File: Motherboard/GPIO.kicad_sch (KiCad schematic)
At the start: 12 parts, among them J19 BM04B-NSHSS-TBT_LF__SN_, J20 BM04B-NSHSS-TBT_LF__SN_, J50 5034801400, J51 5034801400, J52 503480-0800

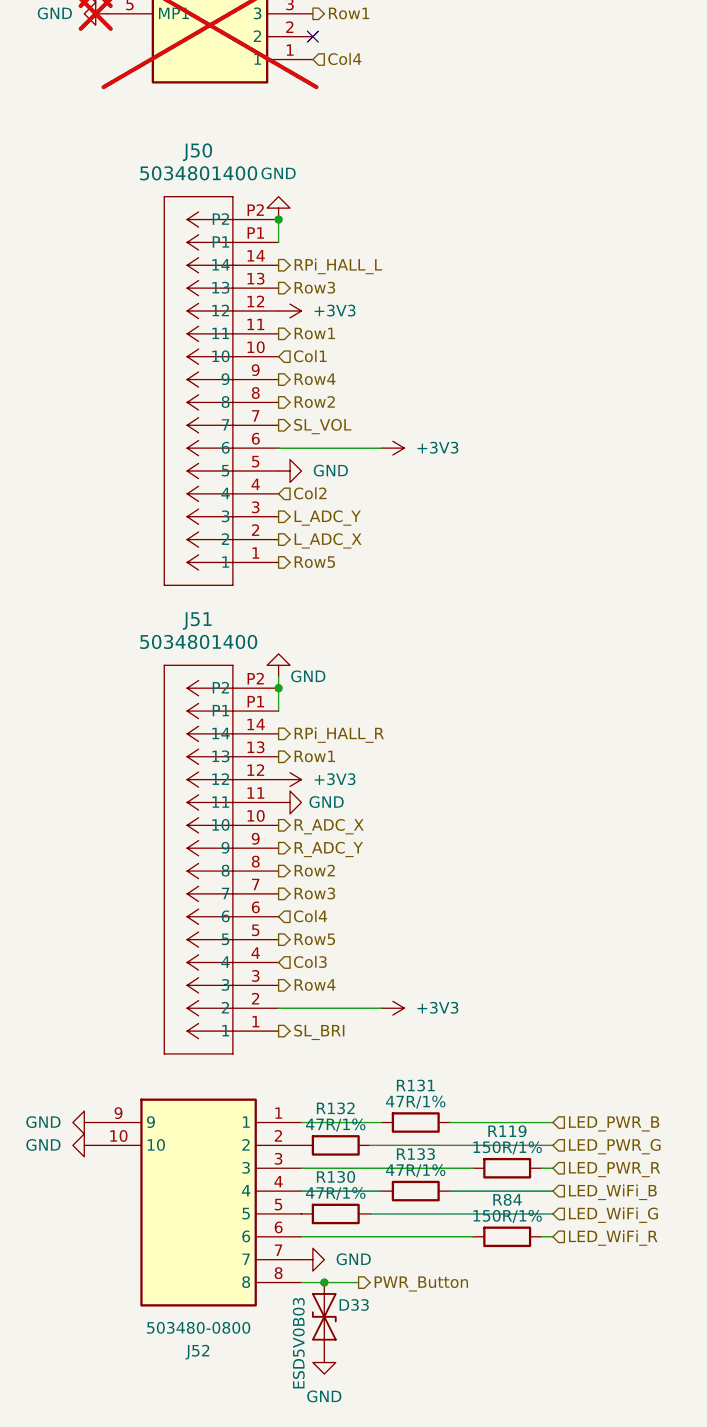
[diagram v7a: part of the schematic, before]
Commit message: Performed analysis of current work. Documented motherboard issues, new revision Todo
- Also updated README
- Other stuff
- 3D Modeling in progress
- Nothing significant done, just want to break the lack of updates.

Project aim to finish before 2027, otherwise no further deadline will be set.
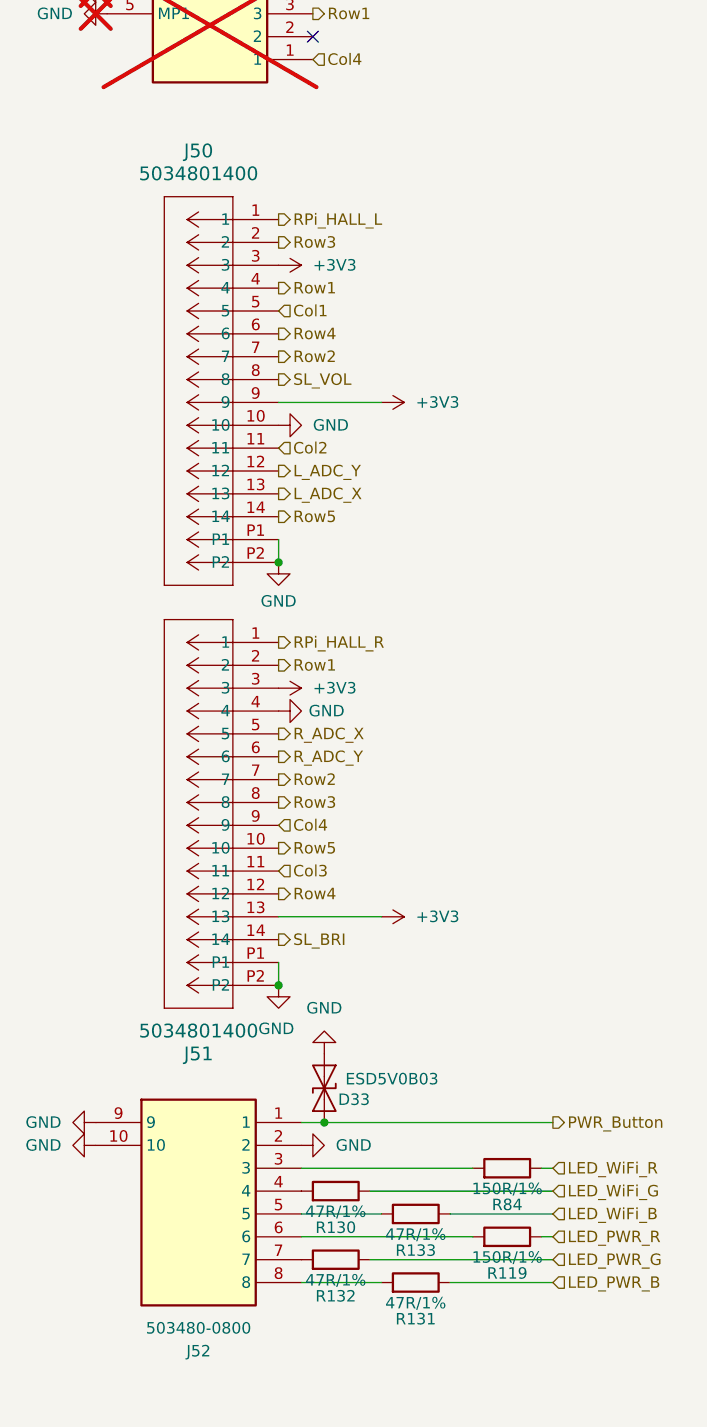
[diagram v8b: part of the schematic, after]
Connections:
- net +3V3: now also J50.3, J50.9, J51.13, J51.3; no longer J50.12, J50.6, J51.12, J51.2
- net Col1: now also J50.5; no longer J50.10
- net Col2: now also J50.11; no longer J50.4
- net Col3: now also J51.11; no longer J51.4
- net Col4: now also J51.9; no longer J51.6
- net GND: now also J50.10, J51.4, J52.2; no longer J50.5, J51.11, J52.7
- net L_ADC_X: now also J50.13; no longer J50.2
- net L_ADC_Y: now also J50.12; no longer J50.3
- net PWR_Button: now also J52.1; no longer J52.8
- net RPi_HALL_L: now also J50.1; no longer J50.14
- net RPi_HALL_R: now also J51.1; no longer J51.14
- net R_ADC_X: now also J51.5; no longer J51.10
- net R_ADC_Y: now also J51.6; no longer J51.9
- net Row1: now also J50.4, J51.2; no longer J50.11, J51.13
- net Row2: now also J50.7, J51.7; no longer J50.8, J51.8
- net Row3: now also J50.2, J51.8; no longer J50.13, J51.7
- net Row4: now also J50.6, J51.12; no longer J50.9, J51.3
- net Row5: now also J50.14, J51.10; no longer J50.1, J51.5
- net SL_BRI: now also J51.14; no longer J51.1
- net SL_VOL: now also J50.8; no longer J50.7
- net at R133.2: now also J52.5; no longer J52.4
- net at R132.2: now also J52.7; no longer J52.2
- net at R131.2: now also J52.8; no longer J52.1
- net at R130.2: now also J52.4; no longer J52.5
- net at R84.2: now also J52.3; no longer J52.6
- net at R119.2: now also J52.6; no longer J52.3
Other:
- moved on the sheet: D33, J50, J51, R119, R130, R131, R132, R133, R84
